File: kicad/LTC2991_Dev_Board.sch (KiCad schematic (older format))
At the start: 15 parts, among them P1 CONN_01X07, P2 CONN_01X07, P3 CONN_02X03, Q1 MMBT3904, Q2 MMBT3904, Q3 MMBT3904, Q4 MMBT3904, U1 LTC2991

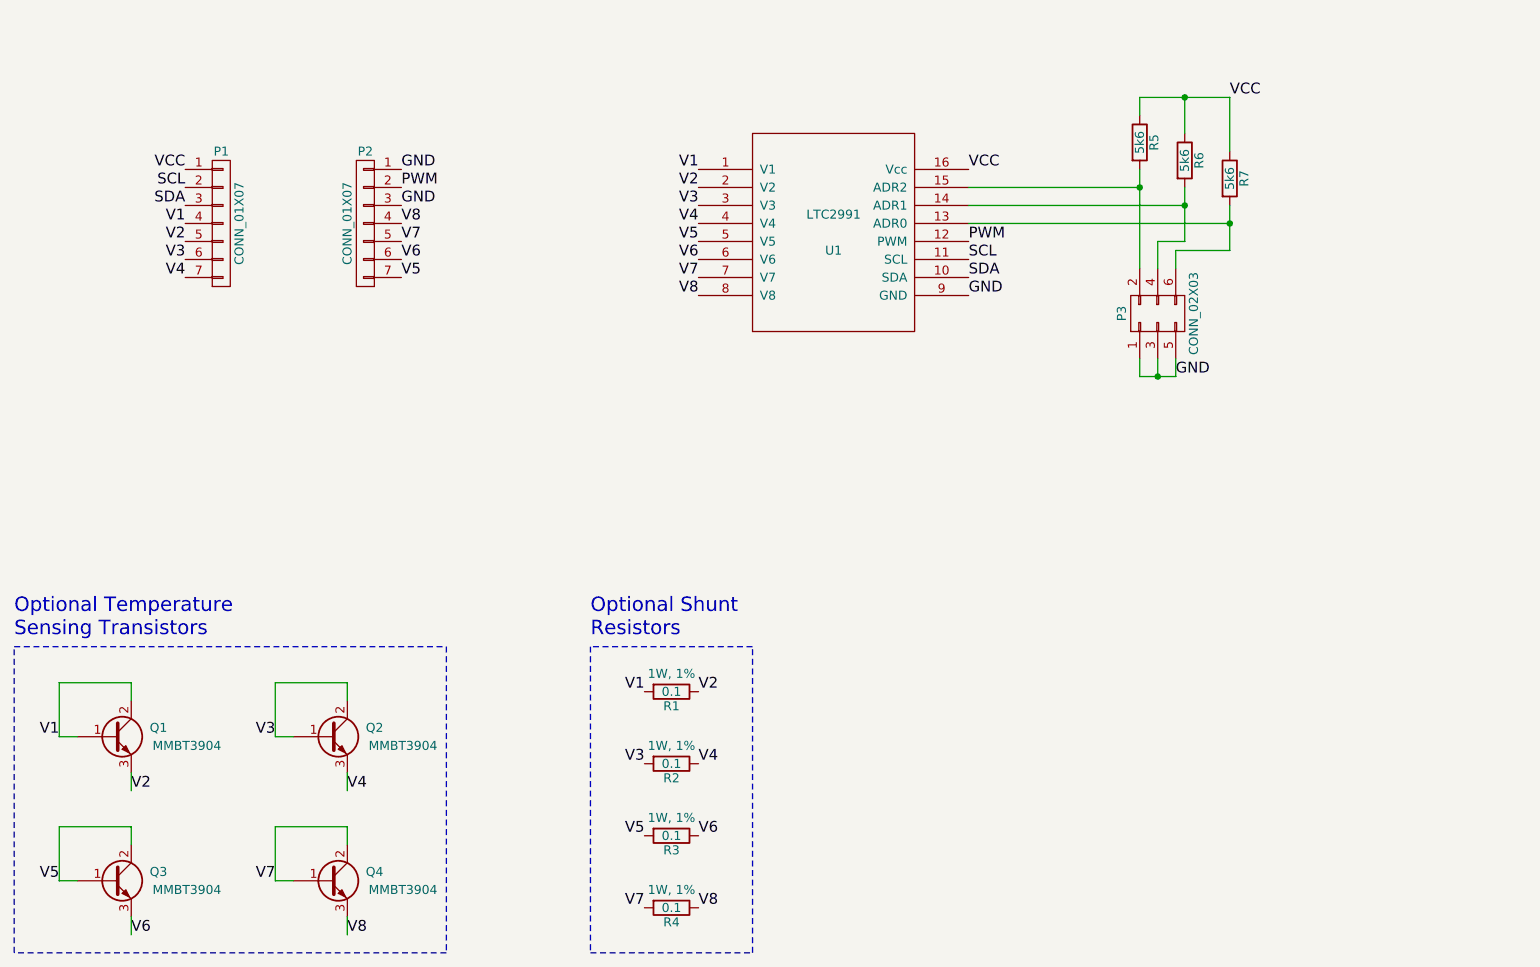
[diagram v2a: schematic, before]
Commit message: Final schematic and PCB layout for Rev. A. Significantly simplified the schematic in order to make the board as compact as possible.
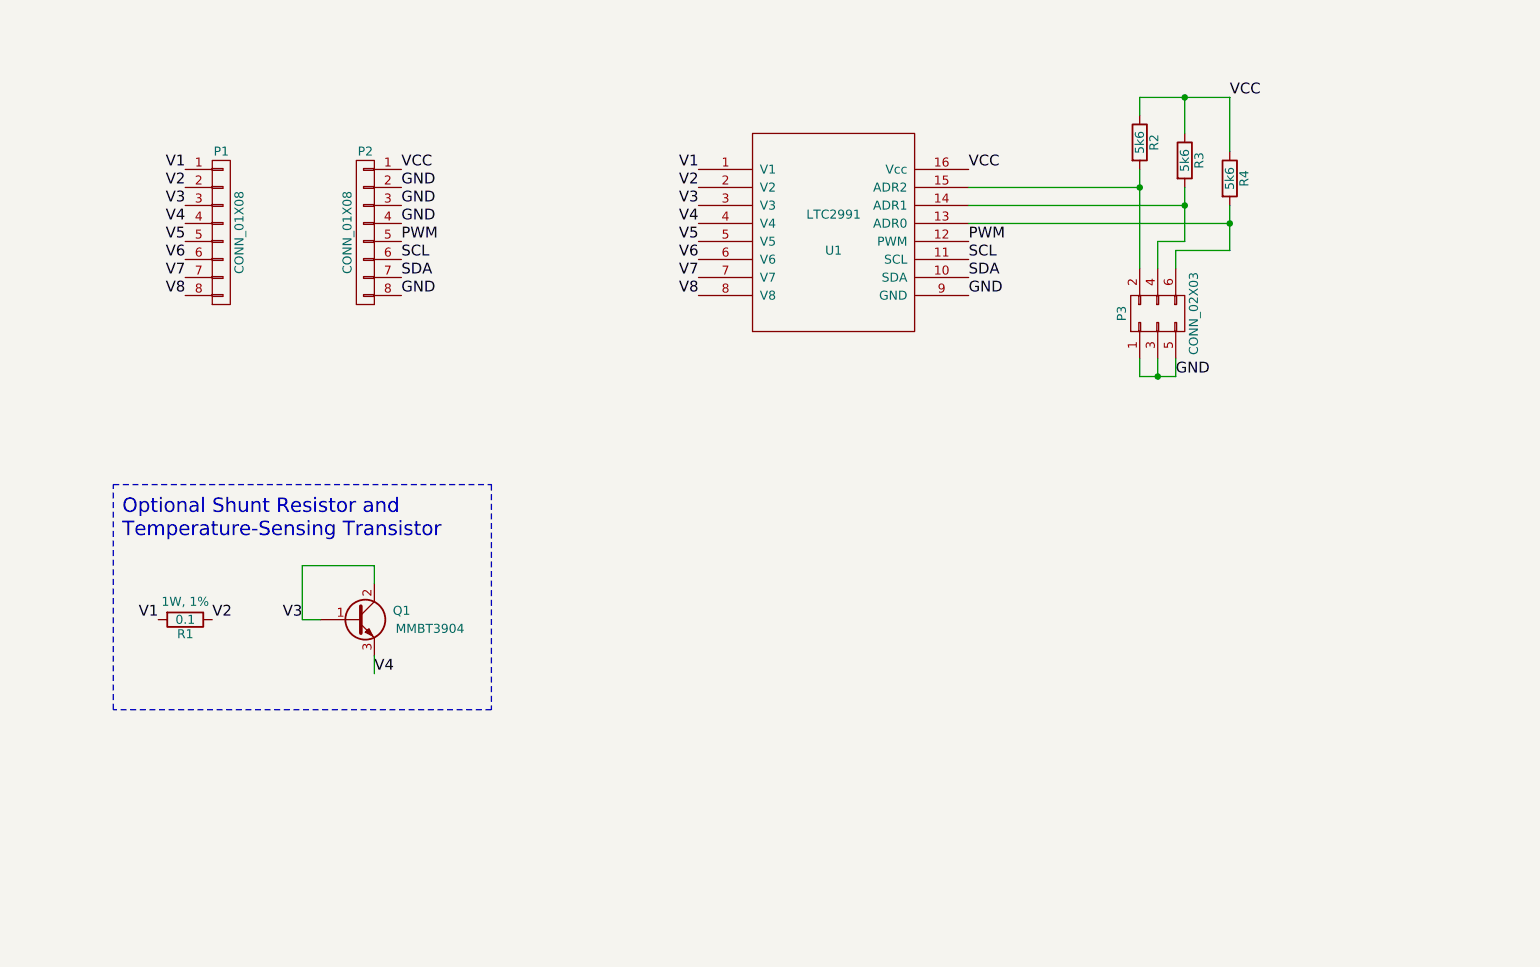
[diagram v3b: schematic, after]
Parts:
- removed P1, P2: CONN_01X07, Pin_Headers:Pin_Header_Straight_1x07, symbol CONN_01X07
- removed Q1, Q3, Q4: MMBT3904, Housings_SOT-23_SOT-143_TSOT-6:SOT-23, symbol Q_NPN_BCE
- removed R2, R3, R4: 0.1, Resistors_SMD:R_1206, symbol R
- added P1, P2: CONN_01X08, Pin_Headers:Pin_Header_Straight_1x08, symbol CONN_01X08
- renumbered Q2 to Q1, R5 to R2, R6 to R3, R7 to R4
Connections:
- net GND: now also P2.2 (P2), P2.3 (P3), P2.4 (P4), P2.8 (P8)
- net PWM: now also P2.5 (P5)
- net SCL: now also P2.6 (P6)
- net SDA: now also P2.7 (P7)
- net V1: now also P1.1 (P1)
- net V2: now also P1.2 (P2)
- net V3: now also P1.3 (P3)
- net V4: now also P1.4 (P4)
- net V5: now also P1.5 (P5)
- net V6: now also P1.6 (P6)
- net V7: now also P1.7 (P7)
- net V8: now also P1.8 (P8)
- net VCC: now also P2.1 (P1)
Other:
- note added: "Optional Shunt Resistor and\nTemperature-Sensing Transistor"
- note removed: "Optional Shunt\nResistors"
- note removed: "Optional Temperature\nSensing Transistors"
- moved on the sheet: Q1, R1
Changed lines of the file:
@@
 Sheet 1 1
 Title "LTC2991 Development Board"
-Date "2015-07-11"
-Rev "1"
+Date "2015-07-15"
+Rev "A"
 Comp "Paul Mullen <pm@nellump.net>"
 Comment1 "<http://www.nellump.net/ltc2991-dev-board>"
@@
 $EndComp
 $Comp
-L R R5
+L R R2
 U 1 1 55A1C08B
 P 7600 2800
-F 0 "R5" V 7680 2800 50  0000 C CNN
+F 0 "R2" V 7680 2800 50  0000 C CNN
 F 1 "5k6" V 7600 2800 50  0000 C CNN
 F 2 "Resistors_SMD:R_0603" V 7530 2800 30  0001 C CNN
@@
 $EndComp
 $Comp
-L R R6
+L R R3
 U 1 1 55A1C0C2
 P 7850 2900
-F 0 "R6" V 7930 2900 50  0000 C CNN
+F 0 "R3" V 7930 2900 50  0000 C CNN
 F 1 "5k6" V 7850 2900 50  0000 C CNN
 F 2 "Resistors_SMD:R_0603" V 7780 2900 30  0001 C CNN
@@
 $EndComp
 $Comp
-L R R7
+L R R4
 U 1 1 55A1C3A3
 P 8100 3000
-F 0 "R7" V 8180 3000 50  0000 C CNN
+F 0 "R4" V 8180 3000 50  0000 C CNN
 F 1 "5k6" V 8100 3000 50  0000 C CNN
 F 2 "Resistors_SMD:R_0603" V 8030 3000 30  0001 C CNN
@@
 V4
 Text Label 2300 2950 2    60   ~ 0
+V1
+Text Label 2300 3050 2    60   ~ 0
+V2
+Text Label 2300 3150 2    60   ~ 0
+V3
+Text Label 3500 3050 0    60   ~ 0
+GND
+Text Label 2300 3250 2    60   ~ 0
+V4
+Text Label 2300 3350 2    60   ~ 0
+V5
+Text Label 2300 3450 2    60   ~ 0
+V6
+Text Label 2300 3550 2    60   ~ 0
+V7
+Text Label 3500 2950 0    60   ~ 0
 VCC
-Text Label 2300 3050 2    60   ~ 0
-SCL
-Text Label 2300 3150 2    60   ~ 0
-SDA
-Text Label 3500 3050 0    60   ~ 0
-PWM
-Text Label 2300 3250 2    60   ~ 0
-V1
-Text Label 2300 3350 2    60   ~ 0
-V2
-Text Label 2300 3450 2    60   ~ 0
-V3
-Text Label 2300 3550 2    60   ~ 0
-V4
-Text Label 3500 2950 0    60   ~ 0
-GND
 Text Label 6650 3650 0    60   ~ 0
 GND
@@
 L R R1
 U 1 1 55A21CED
-P 5000 5850
-F 0 "R1" V 5080 5850 50  0000 C CNN
-F 1 "0.1" V 5000 5850 50  0000 C CNN
-F 2 "Resistors_SMD:R_1206" V 4930 5850 30  0001 C CNN
-F 3 "" H 5000 5850 30  0000 C CNN
-F 4 "1W, 1%" V 4900 5850 50  0000 C CNN "Note"
-	1    5000 5850
+P 2300 5450
+F 0 "R1" V 2380 5450 50  0000 C CNN
+F 1 "0.1" V 2300 5450 50  0000 C CNN
+F 2 "Resistors_SMD:R_1206" V 2230 5450 30  0001 C CNN
+F 3 "" H 2300 5450 30  0000 C CNN
+F 4 "1W, 1%" V 2200 5450 50  0000 C CNN "Note"
+	1    2300 5450
 	0    1    1    0
 $EndComp
@@
 Text Label 5150 3650 2    60   ~ 0
 V8
-$Comp
-L CONN_01X07 P1
-U 1 1 55A22E52
-P 2500 3250
-F 0 "P1" H 2500 3650 50  0000 C CNN
-F 1 "CONN_01X07" V 2600 3250 50  0000 C CNN
-F 2 "Pin_Headers:Pin_Header_Straight_1x07" H 2500 3250 60  0001 C CNN
-F 3 "" H 2500 3250 60  0000 C CNN
-	1    2500 3250
-	1    0    0    -1
-$EndComp
-$Comp
-L CONN_01X07 P2
-U 1 1 55A22EEE
-P 3300 3250
-F 0 "P2" H 3300 3650 50  0000 C CNN
-F 1 "CONN_01X07" V 3400 3250 50  0000 C CNN
-F 2 "Pin_Headers:Pin_Header_Straight_1x07" H 3300 3250 60  0001 C CNN
-F 3 "" H 3300 3250 60  0000 C CNN
-	1    3300 3250
-	-1   0    0    -1
-$EndComp
-Text Label 3500 3550 0    60   ~ 0
-V5
-Text Label 3500 3450 0    60   ~ 0
-V6
-Text Label 3500 3350 0    60   ~ 0
-V7
-Text Label 3500 3250 0    60   ~ 0
-V8
 Text Label 3500 3150 0    60   ~ 0
 GND
-Text Label 4850 5850 2    60   ~ 0
+Text Label 2150 5450 2    60   ~ 0
 V1
-Text Label 5150 5850 0    60   ~ 0
+Text Label 2450 5450 0    60   ~ 0
 V2
-Text Label 2800 6900 2    60   ~ 0
-V7
-Text Label 3200 7200 0    60   ~ 0
-V8
-$Comp
-L Q_NPN_BCE Q4
-U 1 1 55A24DB1
-P 3100 6900
-F 0 "Q4" H 3400 6950 50  0000 R CNN
-F 1 "MMBT3904" H 3700 6850 50  0000 R CNN
-F 2 "Housings_SOT-23_SOT-143_TSOT-6:SOT-23" H 3300 7000 29  0001 C CNN
-F 3 "" H 3100 6900 60  0000 C CNN
-	1    3100 6900
-	1    0    0    -1
-$EndComp
-Wire Wire Line
-	3200 6700 3200 6600
-Wire Wire Line
-	3200 6600 2800 6600
-Wire Wire Line
-	2800 6600 2800 6900
-Wire Wire Line
-	2800 6900 2900 6900
-Wire Wire Line
-	3200 7100 3200 7200
-$Comp
-L R R2
-U 1 1 55A33AA9
-P 5000 6250
-F 0 "R2" V 5080 6250 50  0000 C CNN
-F 1 "0.1" V 5000 6250 50  0000 C CNN
-F 2 "Resistors_SMD:R_1206" V 4930 6250 30  0001 C CNN
-F 3 "" H 5000 6250 30  0000 C CNN
-F 4 "1W, 1%" V 4900 6250 50  0000 C CNN "Note"
-	1    5000 6250
-	0    1    1    0
-$EndComp
-Text Label 4850 6250 2    60   ~ 0
-V3
-Text Label 5150 6250 0    60   ~ 0
-V4
-$Comp
-L R R3
-U 1 1 55A33B91
-P 5000 6650
-F 0 "R3" V 5080 6650 50  0000 C CNN
-F 1 "0.1" V 5000 6650 50  0000 C CNN
-F 2 "Resistors_SMD:R_1206" V 4930 6650 30  0001 C CNN
-F 3 "" H 5000 6650 30  0000 C CNN
-F 4 "1W, 1%" V 4900 6650 50  0000 C CNN "Note"
-	1    5000 6650
-	0    1    1    0
-$EndComp
-Text Label 4850 6650 2    60   ~ 0
-V5
-Text Label 5150 6650 0    60   ~ 0
-V6
-$Comp
-L R R4
-U 1 1 55A33B9A
-P 5000 7050
-F 0 "R4" V 5080 7050 50  0000 C CNN
-F 1 "0.1" V 5000 7050 50  0000 C CNN
-F 2 "Resistors_SMD:R_1206" V 4930 7050 30  0001 C CNN
-F 3 "" H 5000 7050 30  0000 C CNN
-F 4 "1W, 1%" V 4900 7050 50  0000 C CNN "Note"
-	1    5000 7050
-	0    1    1    0
-$EndComp
-Text Label 4850 7050 2    60   ~ 0
-V7
-Text Label 5150 7050 0    60   ~ 0
-V8
-Wire Notes Line
-	5450 7300 5450 5600
-Wire Notes Line
-	5450 5600 4550 5600
-Wire Notes Line
-	4550 5600 4550 7300
-Wire Notes Line
-	4550 7300 5450 7300
-Text Notes 4550 5550 0    80   ~ 0
-Optional Shunt\nResistors
-Text Label 2800 6100 2    60   ~ 0
-V3
-Text Label 3200 6400 0    60   ~ 0
-V4
-$Comp
-L Q_NPN_BCE Q2
-U 1 1 55A33D2F
-P 3100 6100
-F 0 "Q2" H 3400 6150 50  0000 R CNN
-F 1 "MMBT3904" H 3700 6050 50  0000 R CNN
-F 2 "Housings_SOT-23_SOT-143_TSOT-6:SOT-23" H 3300 6200 29  0001 C CNN
-F 3 "" H 3100 6100 60  0000 C CNN
-	1    3100 6100
-	1    0    0    -1
-$EndComp
-Wire Wire Line
-	3200 5900 3200 5800
-Wire Wire Line
-	3200 5800 2800 5800
-Wire Wire Line
-	2800 5800 2800 6100
-Wire Wire Line
-	2800 6100 2900 6100
-Wire Wire Line
-	3200 6300 3200 6400
-Text Label 1600 6900 2    60   ~ 0
-V5
-Text Label 2000 7200 0    60   ~ 0
-V6
-$Comp
-L Q_NPN_BCE Q3
-U 1 1 55A33E3B
-P 1900 6900
-F 0 "Q3" H 2200 6950 50  0000 R CNN
-F 1 "MMBT3904" H 2500 6850 50  0000 R CNN
-F 2 "Housings_SOT-23_SOT-143_TSOT-6:SOT-23" H 2100 7000 29  0001 C CNN
-F 3 "" H 1900 6900 60  0000 C CNN
-	1    1900 6900
-	1    0    0    -1
-$EndComp
-Wire Wire Line
-	2000 6700 2000 6600
-Wire Wire Line
-	2000 6600 1600 6600
-Wire Wire Line
-	1600 6600 1600 6900
-Wire Wire Line
-	1600 6900 1700 6900
-Wire Wire Line
-	2000 7100 2000 7200
-Text Label 1600 6100 2    60   ~ 0
-V1
-Text Label 2000 6400 0    60   ~ 0
-V2
-$Comp
-L Q_NPN_BCE Q1
-U 1 1 55A33E48
-P 1900 6100
-F 0 "Q1" H 2200 6150 50  0000 R CNN
-F 1 "MMBT3904" H 2500 6050 50  0000 R CNN
-F 2 "Housings_SOT-23_SOT-143_TSOT-6:SOT-23" H 2100 6200 29  0001 C CNN
-F 3 "" H 1900 6100 60  0000 C CNN
-	1    1900 6100
-	1    0    0    -1
-$EndComp
-Wire Wire Line
-	2000 5900 2000 5800
-Wire Wire Line
-	2000 5800 1600 5800
-Wire Wire Line
-	1600 5800 1600 6100
-Wire Wire Line
-	1600 6100 1700 6100
-Wire Wire Line
-	2000 6300 2000 6400
-Wire Notes Line
-	3750 7300 1350 7300
-Wire Notes Line
-	1350 7300 1350 5600
-Wire Notes Line
-	1350 5600 3750 5600
-Wire Notes Line
-	3750 5600 3750 7300
-Text Notes 1350 5550 0    80   ~ 0
-Optional Temperature\nSensing Transistors
+Text Notes 1950 5000 0    80   ~ 0
+Optional Shunt Resistor and\nTemperature-Sensing Transistor
 $Comp
 L CONN_02X03 P3
@@
 Text Label 7800 4100 0    60   ~ 0
 GND
+$Comp
+L CONN_01X08 P1
+U 1 1 55A5EA73
+P 2500 3300
+F 0 "P1" H 2500 3750 50  0000 C CNN
+F 1 "CONN_01X08" V 2600 3300 50  0000 C CNN
+F 2 "Pin_Headers:Pin_Header_Straight_1x08" H 2500 3300 60  0001 C CNN
+F 3 "" H 2500 3300 60  0000 C CNN
+	1    2500 3300
+	1    0    0    -1
+$EndComp
+Text Label 2300 3650 2    60   ~ 0
+V8
+$Comp
+L CONN_01X08 P2
+U 1 1 55A5EB80
+P 3300 3300
+F 0 "P2" H 3300 3750 50  0000 C CNN
+F 1 "CONN_01X08" V 3400 3300 50  0000 C CNN
+F 2 "Pin_Headers:Pin_Header_Straight_1x08" H 3300 3300 60  0001 C CNN
+F 3 "" H 3300 3300 60  0000 C CNN
+	1    3300 3300
+	-1   0    0    -1
+$EndComp
+Text Label 3500 3250 0    60   ~ 0
+GND
+Text Label 3500 3350 0    60   ~ 0
+PWM
+Text Label 3500 3450 0    60   ~ 0
+SCL
+Text Label 3500 3550 0    60   ~ 0
+SDA
+Text Label 3500 3650 0    60   ~ 0
+GND
+Wire Wire Line
+	3350 5650 3350 5750
+Wire Wire Line
+	2950 5450 3050 5450
+Wire Wire Line
+	2950 5150 2950 5450
+Wire Wire Line
+	3350 5150 2950 5150
+Wire Wire Line
+	3350 5250 3350 5150
+$Comp
+L Q_NPN_BCE Q1
+U 1 1 55A33D2F
+P 3250 5450
+F 0 "Q1" H 3550 5500 50  0000 R CNN
+F 1 "MMBT3904" H 3850 5400 50  0000 R CNN
+F 2 "Housings_SOT-23_SOT-143_TSOT-6:SOT-23" H 3450 5550 29  0001 C CNN
+F 3 "" H 3250 5450 60  0000 C CNN
+	1    3250 5450
+	1    0    0    -1
+$EndComp
+Text Label 3350 5750 0    60   ~ 0
+V4
+Text Label 2950 5450 2    60   ~ 0
+V3
+Wire Notes Line
+	1900 4700 4000 4700
+Wire Notes Line
+	4000 4700 4000 5950
+Wire Notes Line
+	4000 5950 1900 5950
+Wire Notes Line
+	1900 5950 1900 4700
 $EndSCHEMATC

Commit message: Modified schematic and PCB layout. 1. Added two-pin header for measurement of external current source via    on-board shunt resistor (both optional). 2. Added filter capacitor for IC power. 3. Added filter capacitor for temperature-sensing transistor (both    optional). 4. Placed noise-shielding traces around temperature-sensing    transistor.
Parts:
- added C1: 470p, Capacitors_SMD:C_0402, symbol C_Small
- added C2: 0.1μ, Capacitors_SMD:C_0402, symbol C_Small
- added P4: CONN_SENSE, Pin_Headers:Pin_Header_Straight_1x02, symbol CONN_01X02
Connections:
- net GND: now also C2.2; no longer P2.2 (P2), P2.3 (P3), P2.4 (P4)
- net V1: now also R1.1, P4.1 (P1); no longer R1.2
- net V2: now also R1.2, P4.2 (P2); no longer R1.1
- net V3: now also C1.1
- net V4: now also C1.2
- net VCC: now also C2.1
- new net NC: P2.2 (P2), P2.3 (P3), P2.4 (P4)
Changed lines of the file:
@@
 Sheet 1 1
 Title "LTC2991 Development Board"
-Date "2015-07-15"
-Rev "A"
+Date "2015-07-25"
+Rev "B"
 Comp "Paul Mullen <pm@nellump.net>"
 Comment1 "<http://www.nellump.net/ltc2991-dev-board>"
@@
 Text Label 2300 3150 2    60   ~ 0
 V3
-Text Label 3500 3050 0    60   ~ 0
-GND
 Text Label 2300 3250 2    60   ~ 0
 V4
@@
 F 4 "1W, 1%" V 2200 5450 50  0000 C CNN "Note"
 	1    2300 5450
-	0    1    1    0
-$EndComp
-Wire Wire Line
-	7600 2950 7600 3500
-Wire Wire Line
-	7600 2550 7600 2650
-Wire Wire Line
-	7600 2550 8100 2550
-Connection ~ 7850 2550
+	0    -1   1    0
+$EndComp
 Text Label 5150 3350 2    60   ~ 0
 V5
@@
 Text Label 5150 3650 2    60   ~ 0
 V8
-Text Label 3500 3150 0    60   ~ 0
-GND
 Text Label 2150 5450 2    60   ~ 0
 V1
@@
 	0    -1   -1   0
 $EndComp
-Wire Wire Line
-	7600 3050 6650 3050
-Wire Wire Line
-	7850 3050 7850 3350
-Wire Wire Line
-	7850 3150 6650 3150
-Wire Wire Line
-	8100 3150 8100 3400
-Wire Wire Line
-	8100 3250 6650 3250
-Wire Wire Line
-	7850 2750 7850 2550
-Wire Wire Line
-	8100 2550 8100 2850
-Connection ~ 7600 3050
-Wire Wire Line
-	7850 3350 7700 3350
-Wire Wire Line
-	7700 3350 7700 3500
-Connection ~ 7850 3150
-Wire Wire Line
-	8100 3400 7800 3400
-Wire Wire Line
-	7800 3400 7800 3500
-Connection ~ 8100 3250
-Wire Wire Line
-	7600 4000 7600 4100
-Wire Wire Line
-	7600 4100 7800 4100
-Wire Wire Line
-	7800 4100 7800 4000
-Wire Wire Line
-	7700 4000 7700 4100
-Connection ~ 7700 4100
 Text Label 7800 4100 0    60   ~ 0
 GND
@@
 	-1   0    0    -1
 $EndComp
-Text Label 3500 3250 0    60   ~ 0
-GND
 Text Label 3500 3350 0    60   ~ 0
 PWM
@@
 Text Label 3500 3650 0    60   ~ 0
 GND
-Wire Wire Line
-	3350 5650 3350 5750
-Wire Wire Line
-	2950 5450 3050 5450
-Wire Wire Line
-	2950 5150 2950 5450
-Wire Wire Line
-	3350 5150 2950 5150
-Wire Wire Line
-	3350 5250 3350 5150
 $Comp
 L Q_NPN_BCE Q1
@@
 	1    0    0    -1
 $EndComp
-Text Label 3350 5750 0    60   ~ 0
+Text Label 3350 5800 0    60   ~ 0
 V4
 Text Label 2950 5450 2    60   ~ 0
 V3
+$Comp
+L CONN_01X02 P4
+U 1 1 55B2EA15
+P 2300 5950
+F 0 "P4" H 2300 6100 50  0000 C CNN
+F 1 "CONN_SENSE" V 2400 5950 50  0000 C CNN
+F 2 "Pin_Headers:Pin_Header_Straight_1x02" H 2300 5950 60  0001 C CNN
+F 3 "" H 2300 5950 60  0000 C CNN
+	1    2300 5950
+	0    -1   1    0
+$EndComp
+$Comp
+L C_Small C2
+U 1 1 55B2ECFC
+P 7100 3450
+F 0 "C2" H 7110 3520 50  0000 L CNN
+F 1 "0.1μ" H 7110 3370 50  0000 L CNN
+F 2 "Capacitors_SMD:C_0402" H 7100 3450 60  0001 C CNN
+F 3 "" H 7100 3450 60  0000 C CNN
+	1    7100 3450
+	1    0    0    -1
+$EndComp
+Wire Wire Line
+	7600 2950 7600 3500
+Wire Wire Line
+	7600 2550 7600 2650
+Wire Wire Line
+	7600 2550 8100 2550
+Connection ~ 7850 2550
+Wire Wire Line
+	7600 3050 6650 3050
+Wire Wire Line
+	7850 3050 7850 3350
+Wire Wire Line
+	7850 3150 6650 3150
+Wire Wire Line
+	8100 3150 8100 3400
+Wire Wire Line
+	8100 3250 6650 3250
+Wire Wire Line
+	7850 2750 7850 2550
+Wire Wire Line
+	8100 2550 8100 2850
+Connection ~ 7600 3050
+Wire Wire Line
+	7850 3350 7700 3350
+Wire Wire Line
+	7700 3350 7700 3500
+Connection ~ 7850 3150
+Wire Wire Line
+	8100 3400 7800 3400
+Wire Wire Line
+	7800 3400 7800 3500
+Connection ~ 8100 3250
+Wire Wire Line
+	7600 4000 7600 4100
+Wire Wire Line
+	7600 4100 7800 4100
+Wire Wire Line
+	7800 4100 7800 4000
+Wire Wire Line
+	7700 4000 7700 4100
+Connection ~ 7700 4100
+Wire Wire Line
+	2950 5450 3050 5450
+Wire Wire Line
+	2950 5150 2950 5550
+Wire Wire Line
+	3350 5150 2950 5150
+Wire Wire Line
+	3350 5250 3350 5150
 Wire Notes Line
 	1900 4700 4000 4700
 Wire Notes Line
-	4000 4700 4000 5950
+	4000 4700 4000 6200
 Wire Notes Line
-	4000 5950 1900 5950
+	4000 6200 1900 6200
 Wire Notes Line
-	1900 5950 1900 4700
+	1900 6200 1900 4700
+Wire Wire Line
+	2250 5750 2250 5650
+Wire Wire Line
+	2250 5650 2150 5650
+Wire Wire Line
+	2150 5650 2150 5450
+Wire Wire Line
+	2450 5450 2450 5650
+Wire Wire Line
+	2450 5650 2350 5650
+Wire Wire Line
+	2350 5650 2350 5750
+Wire Wire Line
+	7100 3550 7100 3650
+Wire Wire Line
+	7100 3650 6650 3650
+Wire Wire Line
+	7100 3350 7100 2950
+Wire Wire Line
+	7100 2950 6650 2950
+$Comp
+L C_Small C1
+U 1 1 55B2FA16
+P 2950 5650
+F 0 "C1" H 2960 5720 50  0000 L CNN
+F 1 "470p" H 2960 5570 50  0000 L CNN
+F 2 "Capacitors_SMD:C_0402" H 2950 5650 60  0001 C CNN
+F 3 "" H 2950 5650 60  0000 C CNN
+	1    2950 5650
+	1    0    0    -1
+$EndComp
+Connection ~ 2950 5450
+Wire Wire Line
+	3350 5650 3350 5850
+Wire Wire Line
+	3350 5850 2950 5850
+Wire Wire Line
+	2950 5850 2950 5750
+Text Label 3500 3250 0    60   ~ 0
+NC
+Text Label 3500 3150 0    60   ~ 0
+NC
+Text Label 3500 3050 0    60   ~ 0
+NC
 $EndSCHEMATC
